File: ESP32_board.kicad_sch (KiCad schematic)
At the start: 8 parts, among them J1 SS-52400-002, J2 B2B-PH-SM4-TB, U1 MCP73871

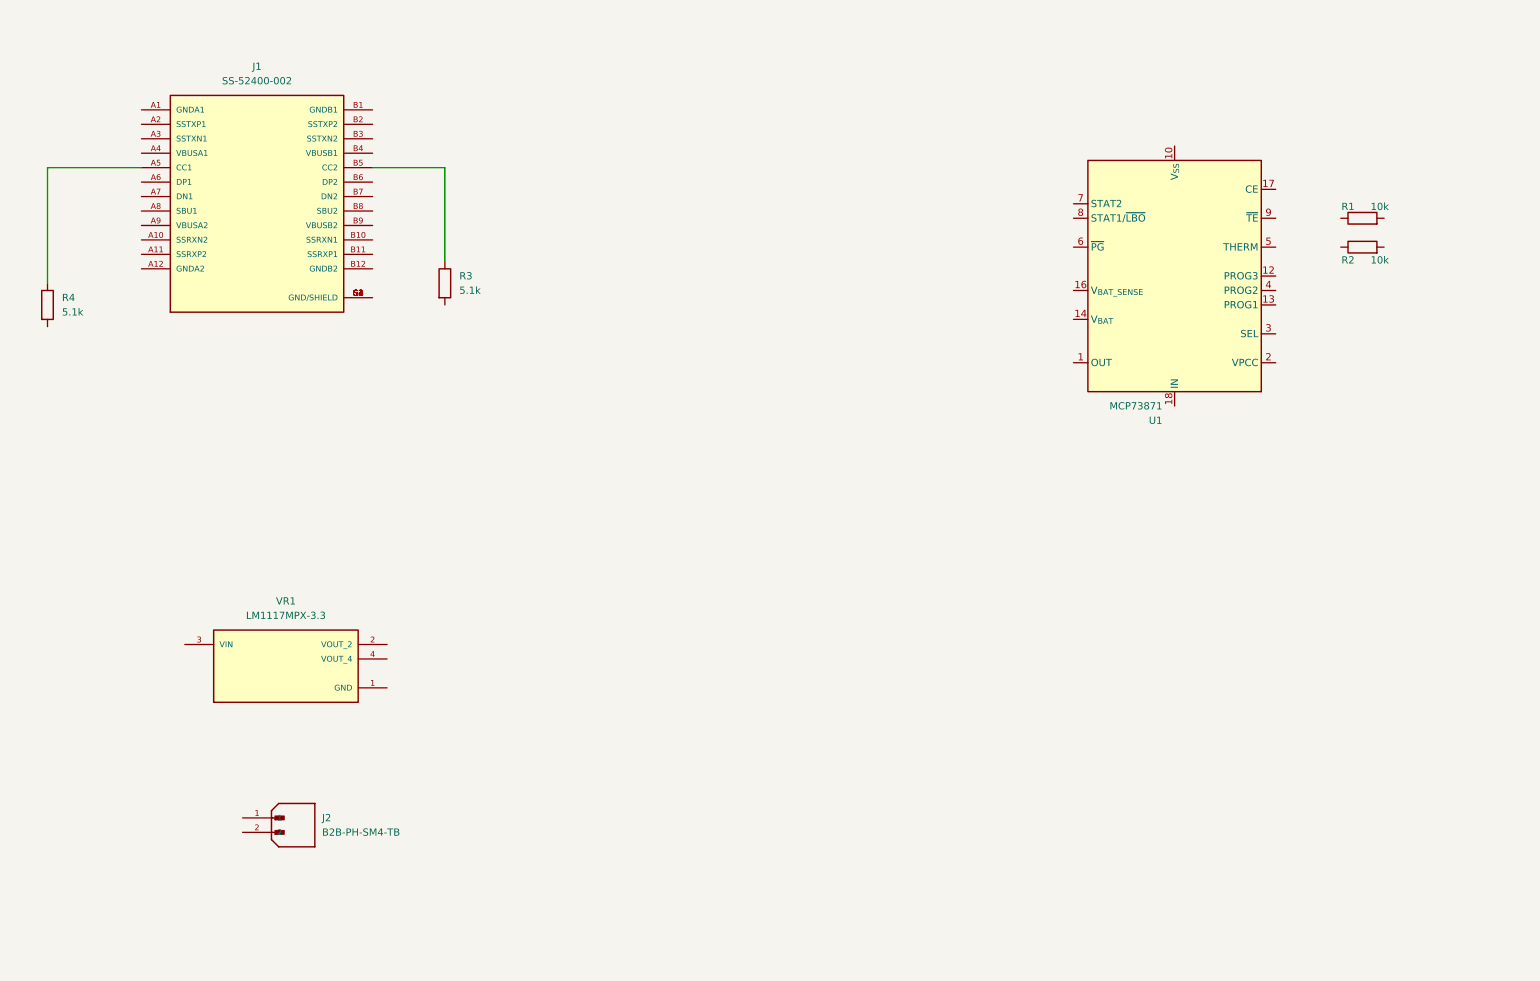
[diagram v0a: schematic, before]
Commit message: finished USB connector and Lipo charger schematic
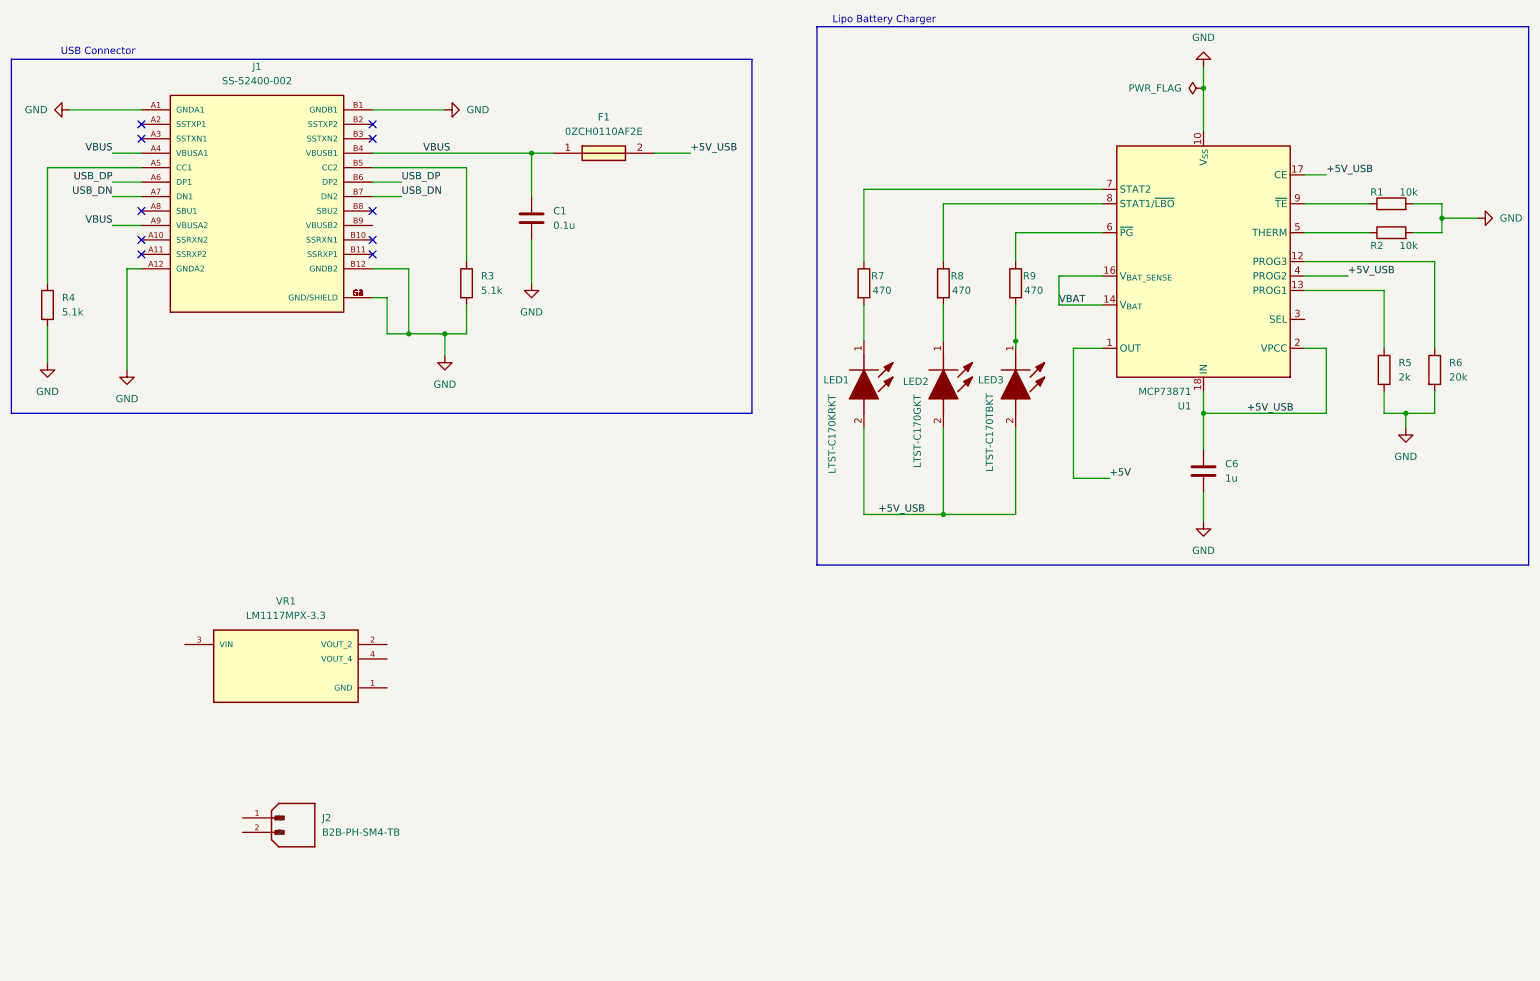
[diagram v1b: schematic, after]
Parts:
- added C1: 0.1u, symbol Device:C
- added C6: 1u, symbol Device:C
- added F1: 0ZCH0110AF2E, FUSC3226X100N, symbol 0ZCH0110AF2E:0ZCH0110AF2E
- added LED1: LTST-C170KRKT, LEDC2012X120N, symbol LTST-C170KRKT:LTST-C170KRKT
- added LED2: LTST-C170GKT, LEDC2012X120N, symbol LTST-C170GKT:LTST-C170GKT
- added LED3: LTST-C170TBKT, LEDC2012X120N, symbol LTST-C170TBKT:LTST-C170TBKT
- added R5: 2k, symbol Device:R
- added R6: 20k, symbol Device:R
- added R7, R8, R9: 470, symbol Device:R
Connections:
- net at R2.1: now also U1.5 (THERM)
- net GND: now reaches R2.2
- net GND: now also J1.A1 (GNDA1), J1.A12 (GNDA2), J1.B1 (GNDB1), J1.B12 (GNDB2), J1.G1 (GND/SHIELD), J1.G2 (GND/SHIELD), J1.G3 (GND/SHIELD), J1.G4 (GND/SHIELD), J1.S1 (GND/SHIELD), J1.S2 (GND/SHIELD), J1.S3 (GND/SHIELD), J1.S4 (GND/SHIELD), R1.2, R3.2, R4.2, U1.10 (V_{SS}), U1.11 (V_{SS}), U1.21 (V_{SS}), C1.2, C6.2, R5.2, R6.2
- net +5V: now reaches U1.1 (OUT), U1.20 (OUT)
- net at U1.12 (PROG3): now also R6.1
- net at U1.13 (PROG1): now also R5.1
- net VBAT: now reaches U1.14 (V_{BAT}), U1.15 (V_{BAT})
- net VBAT: now also U1.16 (V_{BAT_SENSE})
- net +5V_USB: now reaches U1.17 (CE)
- net +5V_USB: now also U1.18 (IN), U1.19 (IN), U1.2 (VPCC), U1.4 (PROG2), C6.1, F1.2, LED1.2 (A), LED2.2 (A), LED3.2 (A)
- net at U1.6 (~{PG}): now also R9.1
- net at U1.7 (STAT2): now also R7.1
- net at U1.8 (STAT1/~{LBO}): now also R8.1
- net at U1.9 (~{TE}): now also R1.1
- net VBUS: now reaches J1.A4 (VBUSA1)
- net VBUS: now also J1.A9 (VBUSA2), J1.B4 (VBUSB1), C1.1, F1.1
- net USB_DP: now reaches J1.A6 (DP1)
- net USB_DP: now also J1.B6 (DP2)
- net USB_DN: now reaches J1.A7 (DN1)
- net USB_DN: now also J1.B7 (DN2)
- new net: LED3.1 (K), R9.2
- new net: LED1.1 (K), R7.2
- new net: LED2.1 (K), R8.2
- no-connect marks 0 -> 10
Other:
- note added: "Lipo Battery Charger"
- note added: "USB Connector"
- moved on the sheet: R1, R2, R3, U1

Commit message: finished LDO and battery connector schematic
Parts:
- added C2, C5: 0.1u, symbol Device:C
- added C3, C4: 10u, symbol Device:C_Polarized
- added LED4: LTST-C170KRKT, LEDC2012X120N, symbol LTST-C170KRKT:LTST-C170KRKT
- added R10: 470, symbol Device:R
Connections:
- net +5V: now also VR1.3 (VIN), C2.1, C3.1
- net GND: now also J2.1, VR1.1 (GND), C2.2, C3.2, C4.2, C5.2, R10.1
- net VBAT: now also J2.2
- net THERM: now reaches R2.1, U1.5 (THERM)
- net PROG3: now reaches R6.1, U1.12 (PROG3)
- net PROG1: now reaches R5.1, U1.13 (PROG1)
- net CHARGING: now reaches R9.1, U1.6 (~{PG})
- net at R9.2: now also LED1.1 (K); no longer LED3.1 (K)
- net CHARGING_POWER_GOOD: now reaches R7.1, U1.7 (STAT2)
- net CHARGED: now reaches R8.1, U1.8 (STAT1/~{LBO})
- net TE~: now reaches R1.1, U1.9 (~{TE})
- net at R7.2: now also LED3.1 (K); no longer LED1.1 (K)
- net +3V3: now reaches VR1.2 (VOUT_2)
- net +3V3: now also VR1.4 (VOUT_4), C4.1, C5.1, LED4.2 (A)
- new net PWR_LED: LED4.1 (K), R10.2
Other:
- added sheet ESP32-C3-02 (ESP32-C3-02.kicad_sch)
- note added: "Battery JST Connector"
- note added: "LDO 5V -> 3.3V"
- note added: "Power LED"
- moved on the sheet: J2, LED1, LED2, LED3, R8, VR1

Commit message: finished USB/UART bridge and ESP32 schematic
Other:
- sheet ESP32-C3-02 ports: added USB_DN, USB_DP, VBUS; removed none
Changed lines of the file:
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@@
 	(wire
 		(pts
+			(xy 166.37 138.43) (xy 170.815 138.43)
+		)
+		(stroke
+			(width 0)
+			(type default)
+		)
+	)
+	(wire
+		(pts
 			(xy 95.25 67.31) (xy 95.25 50.8)
 		)
@@
 	(wire
 		(pts
+			(xy 166.37 143.51) (xy 170.815 143.51)
+		)
+		(stroke
+			(width 0)
+			(type default)
+		)
+	)
+	(wire
+		(pts
 			(xy 81.28 123.19) (xy 85.09 123.19)
 		)
@@
 	(wire
 		(pts
+			(xy 166.37 132.08) (xy 170.815 132.08)
+		)
+		(stroke
+			(width 0)
+			(type default)
+		)
+	)
+	(wire
+		(pts
 			(xy 52.07 170.18) (xy 59.69 170.18)
 		)
@@
 		)
 	)
+	(label "USB_DN"
+		(at 166.37 132.08 180)
+		(effects
+			(font
+				(size 1.27 1.27)
+			)
+			(justify right bottom)
+		)
+	)
 	(label "+5V_USB"
 		(at 246.38 52.07 0)
@@
 		)
 	)
+	(label "USB_DP"
+		(at 166.37 138.43 180)
+		(effects
+			(font
+				(size 1.27 1.27)
+			)
+			(justify right bottom)
+		)
+	)
+	(label "VBUS"
+		(at 166.37 143.51 180)
+		(effects
+			(font
+				(size 1.27 1.27)
+			)
+			(justify right bottom)
+		)
+	)
 	(label "PWR_LED"
 		(at 123.19 173.99 0)
@@
 		)
 		(fill
-			(color 0 0 0 0)
+			(color 0 0 255 0.4588235294)
 		)
 		(property "Sheetname" "ESP32-C3-02"
@@
 			)
 		)
+		(pin "USB_DN" input
+			(at 170.815 132.08 180)
+			(effects
+				(font
+					(size 1.27 1.27)
+				)
+				(justify left)
+			)
+		)
+		(pin "USB_DP" input
+			(at 170.815 138.43 180)
+			(effects
+				(font
+					(size 1.27 1.27)
+				)
+				(justify left)
+			)
+		)
+		(pin "VBUS" input
+			(at 170.815 143.51 180)
+			(effects
+				(font
+					(size 1.27 1.27)
+				)
+				(justify left)
+			)
+		)

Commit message: setup net classes and started layout
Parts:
- C1, C2, C5, C6: footprint (none) -> Capacitor_SMD:C_0805_2012Metric
- C3, C4: footprint (none) -> ESP32_project_Footprints:T491A
- F1: footprint FUSC3226X100N -> ESP32_project_Footprints:FUSC3226X100N
- LED1, LED2, LED3, LED4: footprint LEDC2012X120N -> ESP32_project_Footprints:LEDC2012X120N
- R1, R10, R2, R3, R4, R5, R6, R7, R8, R9: footprint (none) -> Resistor_SMD:R_0805_2012Metric
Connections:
- net GND: now also U1.3 (SEL)
- net VBUS: now also J1.B9 (VBUSB2)

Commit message: imported all footprints into layout
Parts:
- J1: footprint SS-52400-002:BELFUSE_SS-52400-002 -> ESP32_project_Footprints:BELFUSE_SS-52400-002; Availability In Stock -> (none); Package None -> (none); Price None -> (none)
- J2: footprint B2B-PH-SM4-TB:JST_B2B-PH-SM4-TB -> ESP32_project_Footprints:JST_B2B-PH-SM4-TB; Availability In Stock -> (none); Package NON STANDARD-2 JST -> (none); Price None -> (none)
- VR1: footprint LM1117MPX-3.3:VREG_LM1117MPX-3.3 -> ESP32_project_Footprints:VREG_LM1117MPX-3.3; Availability In Stock -> (none); Package SOT-223-4 ON Semiconductor -> (none); Price None -> (none)
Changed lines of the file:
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@@
 			)
 		)
-		(property "Footprint" "B2B-PH-SM4-TB:JST_B2B-PH-SM4-TB"
+		(property "Footprint" "ESP32_project_Footprints:JST_B2B-PH-SM4-TB"
 			(at 46.99 170.18 0)
 			(hide yes)
@@
 			)
 		)
-		(property "Package" "NON STANDARD-2 JST"
-			(at 46.99 170.18 0)
-			(hide yes)
-			(show_name no)
-			(do_not_autoplace no)
-			(effects
-				(font
-					(size 1.27 1.27)
-				)
-				(justify bottom)
-			)
-		)
-		(property "Price" "None"
-			(at 46.99 170.18 0)
-			(hide yes)
-			(show_name no)
-			(do_not_autoplace no)
-			(effects
-				(font
-					(size 1.27 1.27)
-				)
-				(justify bottom)
-			)
-		)
 		(property "Check_prices" "https://www.snapeda.com/parts/B2B-PH-SM4-TB/JST/view-part/?ref=eda"
 			(at 46.99 170.18 0)
@@
 		)
 		(property "MP" "B2B-PH-SM4-TB"
-			(at 46.99 170.18 0)
-			(hide yes)
-			(show_name no)
-			(do_not_autoplace no)
-			(effects
-				(font
-					(size 1.27 1.27)
-				)
-				(justify bottom)
-			)
-		)
-		(property "Availability" "In Stock"
 			(at 46.99 170.18 0)
 			(hide yes)
@@
 			)
 		)
-		(property "Footprint" "SS-52400-002:BELFUSE_SS-52400-002"
+		(property "Footprint" "ESP32_project_Footprints:BELFUSE_SS-52400-002"
 			(at 58.42 55.88 0)
 			(hide yes)
@@
 			)
 		)
-		(property "Package" "None"
-			(at 58.42 55.88 0)
-			(hide yes)
-			(show_name no)
-			(do_not_autoplace no)
-			(effects
-				(font
-					(size 1.27 1.27)
-				)
-				(justify bottom)
-			)
-		)
-		(property "Price" "None"
-			(at 58.42 55.88 0)
-			(hide yes)
-			(show_name no)
-			(do_not_autoplace no)
-			(effects
-				(font
-					(size 1.27 1.27)
-				)
-				(justify bottom)
-			)
-		)
 		(property "Check_prices" "https://www.snapeda.com/parts/SS-52400-002/Bel+Circuit+Protection/view-part/?ref=eda"
 			(at 58.42 55.88 0)
@@
 		)
 		(property "MP" "SS-52400-002"
-			(at 58.42 55.88 0)
-			(hide yes)
-			(show_name no)
-			(do_not_autoplace no)
-			(effects
-				(font
-					(size 1.27 1.27)
-				)
-				(justify bottom)
-			)
-		)
-		(property "Availability" "In Stock"
 			(at 58.42 55.88 0)
 			(hide yes)
@@
 			)
 		)
-		(property "Footprint" "LM1117MPX-3.3:VREG_LM1117MPX-3.3"
+		(property "Footprint" "ESP32_project_Footprints:VREG_LM1117MPX-3.3"
 			(at 63.5 123.19 0)
 			(hide yes)
@@
 			)
 		)
-		(property "Package" "SOT-223-4 ON Semiconductor"
-			(at 63.5 123.19 0)
-			(hide yes)
-			(show_name no)
-			(do_not_autoplace no)
-			(effects
-				(font
-					(size 1.27 1.27)
-				)
-				(justify bottom)
-			)
-		)
 		(property "Check_prices" "https://www.snapeda.com/parts/LM1117MPX-33NOPB/Onsemi/view-part/?ref=eda"
 			(at 63.5 123.19 0)
@@
 			)
 		)
-		(property "Price" "None"
-			(at 63.5 123.19 0)
-			(hide yes)
-			(show_name no)
-			(do_not_autoplace no)
-			(effects
-				(font
-					(size 1.27 1.27)
-				)
-				(justify bottom)
-			)
-		)
 		(property "SnapEDA_Link" "https://www.snapeda.com/parts/LM1117MPX-33NOPB/Onsemi/view-part/?ref=snap"
 			(at 63.5 123.19 0)
@@
 			(at 63.5 123.19 0)
 			(hide yes)
-			(show_name no)
-			(do_not_autoplace no)
-			(effects
-				(font
-					(size 1.27 1.27)
-				)
-				(justify bottom)
-			)
-		)
-		(property "Availability" "In Stock"
-			(at 63.5 123.19 0)
-			(hide yes)

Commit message: finalized edge cuts and component placement
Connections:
- net CC2: now reaches J1.B5 (CC2), R3.1
- net CC1: now reaches J1.A5 (CC1), R4.1
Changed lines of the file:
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@@
+		)
+	)
+	(label "CC1"
+		(at 25.4 50.8 0)
+		(effects
+			(font
+				(size 1.27 1.27)
+			)
+			(justify left bottom)
 		)
 	)
@@
 		(effects
 			(font
+				(size 1.27 1.27)
+			)
+			(justify left bottom)
+		)
+	)
+	(label "CC2"
+		(at 83.82 50.8 0)
+		(effects
+			(font

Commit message: added pot to mic amp, made buttons bigger
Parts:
- added F2: 0ZCH0110AF2E, ESP32_project_Footprints:FUSC3226X100N, symbol 0ZCH0110AF2E:0ZCH0110AF2E
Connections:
- net +5V: now also F2.1; no longer U1.1 (OUT), U1.20 (OUT)
- new net: F2.2, U1.1 (OUT), U1.20 (OUT)
